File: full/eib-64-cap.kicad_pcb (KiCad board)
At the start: 2 copper layers, 140.4 x 111.2 mm, 36 parts, among them J1 DF40C-70DP-0.4V(51), J10 DF40C-70DP-0.4V(51), J11 DF40C-70DP-0.4V(51), J12 DF40C-70DP-0.4V(51), J2 DF40C-70DP-0.4V(51), J3 DF40C-70DP-0.4V(51), J4 DF40C-70DP-0.4V(51), J5 DF40C-70DP-0.4V(51), J6 DF40C-70DP-0.4V(51), J7 DF40C-70DP-0.4V(51), J8 DF40C-70DP-0.4V(51), J9 DF40C-70DP-0.4V(51)

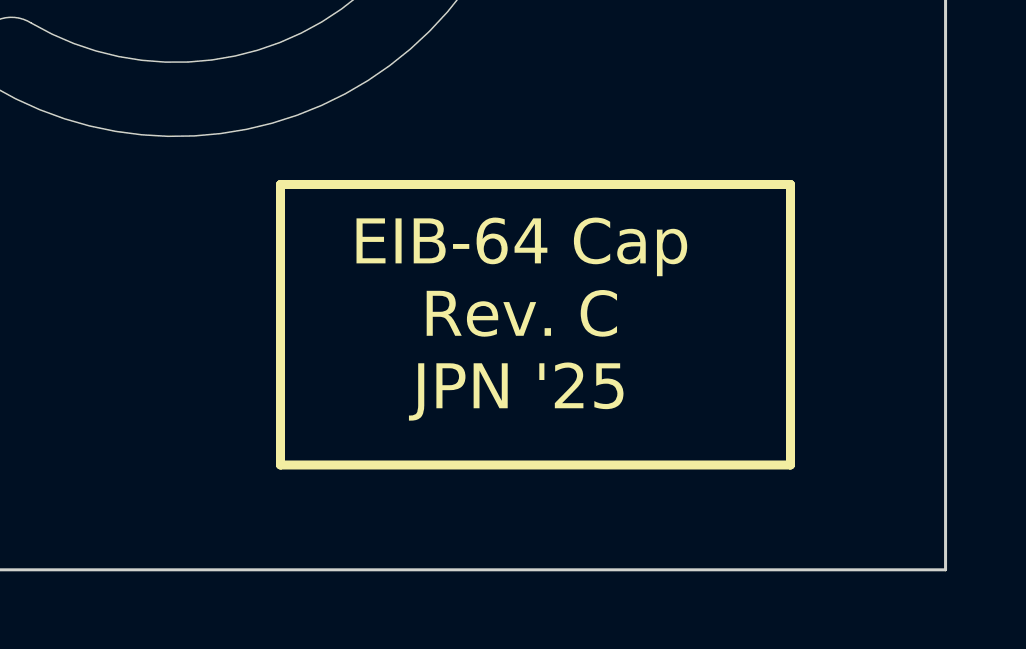
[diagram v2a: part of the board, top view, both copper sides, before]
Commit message: Remov JPN from on-board title box
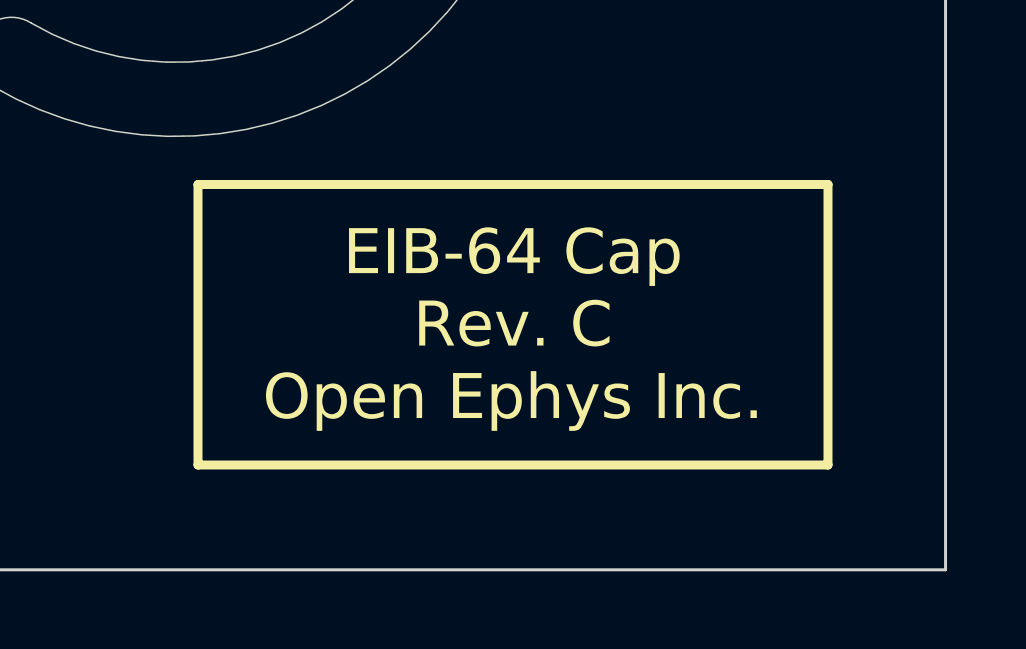
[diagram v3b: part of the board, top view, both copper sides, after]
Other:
- board text added: "EIB-64 Cap Rev. C Open Ephys Inc."
- board text removed: "EIB-64 Cap Rev. C JPN '25"
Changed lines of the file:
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@@
 	)
 	(gr_rect
-		(start 175.03137 141.856371)
-		(end 192.03137 151.206371)
+		(start 172.28137 141.856371)
+		(end 193.28137 151.206371)
 		(stroke
 			(width 0.3)
@@
 		)
 	)
-	(gr_text "EIB-64 Cap\nRev. C\nJPN '25"
-		(at 183.03137 146.206371 0)
+	(gr_text "EIB-64 Cap\nRev. C\nOpen Ephys Inc."
+		(at 182.78137 146.531371 0)
 		(layer "F.SilkS")
 		(effects
